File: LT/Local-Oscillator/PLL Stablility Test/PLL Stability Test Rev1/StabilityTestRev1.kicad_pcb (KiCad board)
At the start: 2 copper layers, 12 parts, among them J1 Conn_Coaxial, J11 Conn_Coaxial, J2 Conn_Coaxial, J6 Conn_01x02_Male, J9 Conn_01x03_Male, U3 LMH6611, U4 LMH6611

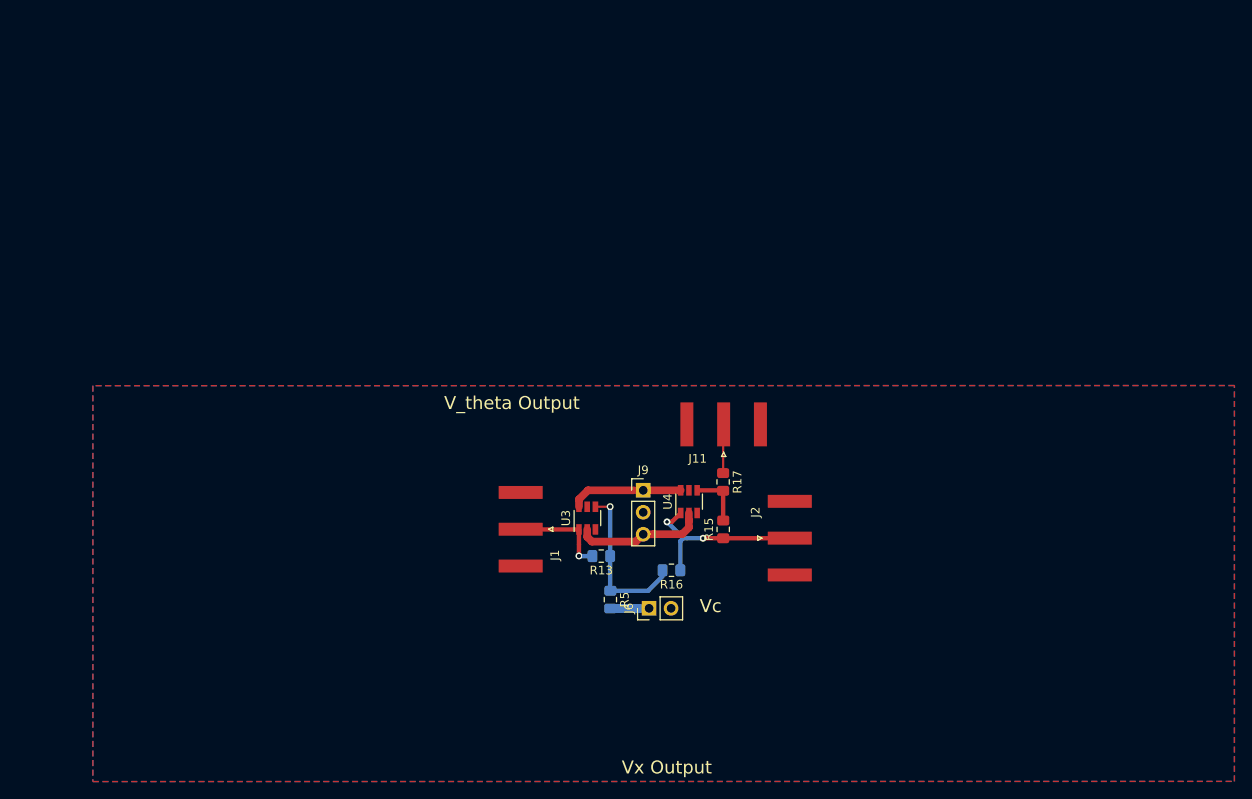
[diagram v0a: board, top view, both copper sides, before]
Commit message: Added Capacitors to the Op-Amp board
I added some capacitors to the Op-Amp test board
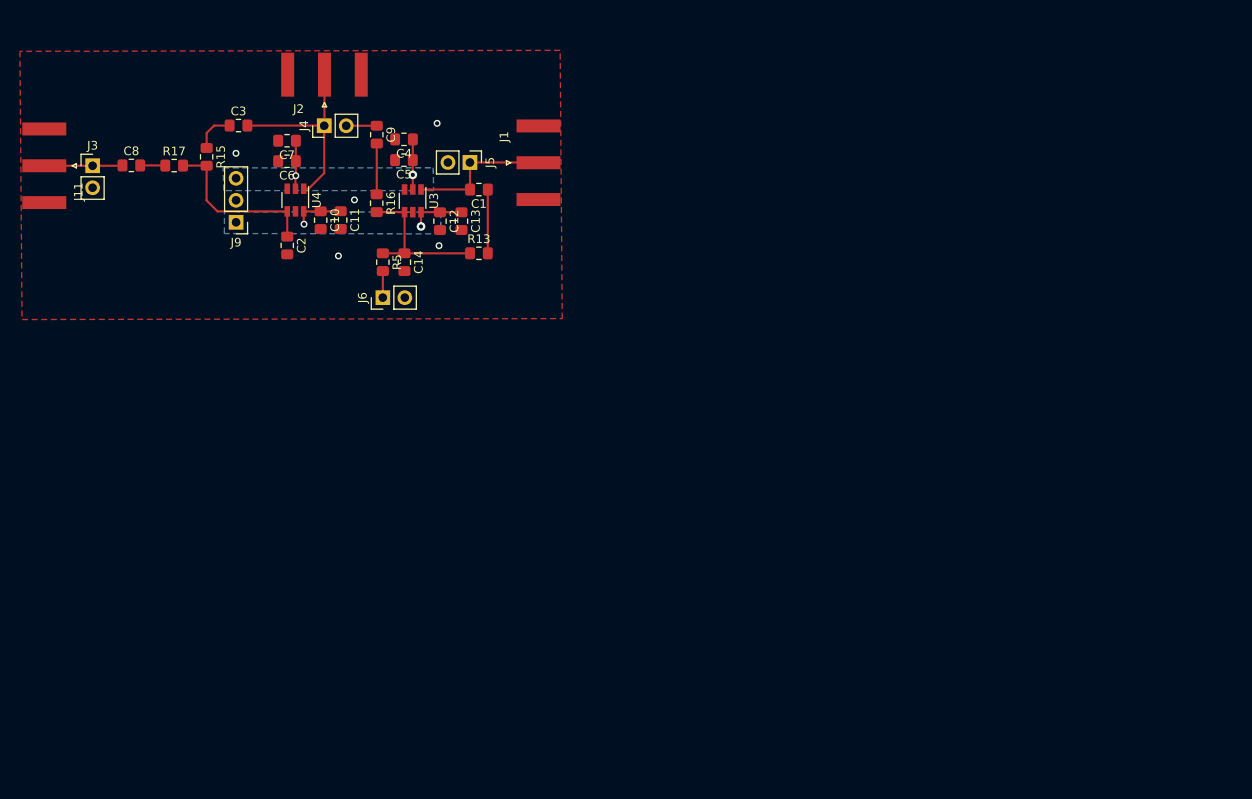
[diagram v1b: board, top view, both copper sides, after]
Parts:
- added C1: 150pF, Capacitor_SMD:C_0805_2012Metric_Pad1.15x1.40mm_HandSolder, F.Cu at (100.7, 53.6)
- added C10: 0.1uF, Capacitor_SMD:C_0805_2012Metric_Pad1.15x1.40mm_HandSolder, F.Cu at (82.4, 57.1)
- added C11: 10uF, Capacitor_SMD:C_0805_2012Metric_Pad1.15x1.40mm_HandSolder, F.Cu at (84.7, 57.1)
- added C12: 0.1uF, Capacitor_SMD:C_0805_2012Metric_Pad1.15x1.40mm_HandSolder, F.Cu at (96.2, 57.2)
- added C13: 10uF, Capacitor_SMD:C_0805_2012Metric_Pad1.15x1.40mm_HandSolder, F.Cu at (98.7, 57.2)
- added C14: 1nF, Capacitor_SMD:C_0805_2012Metric_Pad1.15x1.40mm_HandSolder, F.Cu at (92.1, 62.0)
- added C2: 1nF, Capacitor_SMD:C_0805_2012Metric_Pad1.15x1.40mm_HandSolder, F.Cu at (78.6, 60.0)
- added C3: 150pF, Capacitor_SMD:C_0805_2012Metric_Pad1.15x1.40mm_HandSolder, F.Cu at (72.9, 46.2)
- added C4: 0.1uF, Capacitor_SMD:C_0805_2012Metric_Pad1.15x1.40mm_HandSolder, F.Cu at (92.1, 47.8)
- added C5: 0.1uF, Capacitor_SMD:C_0805_2012Metric_Pad1.15x1.40mm_HandSolder, F.Cu at (92.0, 50.2)
- added C6: 10uF, Capacitor_SMD:C_0805_2012Metric_Pad1.15x1.40mm_HandSolder, F.Cu at (78.5, 50.3)
- added C7: 10uF, Capacitor_SMD:C_0805_2012Metric_Pad1.15x1.40mm_HandSolder, F.Cu at (78.5, 47.9)
- added C8: 1uF, Capacitor_SMD:C_0805_2012Metric_Pad1.15x1.40mm_HandSolder, F.Cu at (60.6, 50.8)
- added C9: 1uF, Capacitor_SMD:C_0805_2012Metric_Pad1.15x1.40mm_HandSolder, F.Cu at (88.9, 47.2)
- added J3: Conn_01x02_Male, Connector_PinHeader_2.54mm:PinHeader_1x02_P2.54mm_Vertical, F.Cu at (56.1, 50.8)
- added J4: Conn_01x02_Male, Connector_PinHeader_2.54mm:PinHeader_1x02_P2.54mm_Vertical, F.Cu at (82.8, 46.2)
- added J5: Conn_01x02_Male, Connector_PinHeader_2.54mm:PinHeader_1x02_P2.54mm_Vertical, F.Cu at (99.7, 50.4)
- moved J11 84.0 mm to (50.5, 50.8), turned to 180 degrees
- moved J2 75.9 mm to (82.9, 40.3), turned to 90 degrees
- moved R15 73.6 mm to (69.3, 49.8), turned to 270 degrees
- moved R17 73.2 mm to (65.5, 50.8), turned to 0 degrees
- moved U4 57.3 mm to (79.5, 54.8), turned to 270 degrees
- moved J9 56.3 mm to (72.7, 57.4), turned to 180 degrees
- moved R16 54.4 mm to (88.9, 55.1), turned to 270 degrees
- moved J6 47.3 mm to (89.6, 66.0)
- moved R5 47.0 mm to (89.6, 62.0)
- moved J1 42.4 mm to (107.6, 50.5), turned to 0 degrees
- moved U3 41.8 mm to (93.1, 54.9), turned to 270 degrees
- moved R13 37.7 mm to (100.7, 60.9), turned to 0 degrees
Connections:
- J1 pad 1: Net-(J1-Pad1) -> Net-(C1-Pad2)
- J11 pad 1: Net-(J11-Pad1) -> Net-(C8-Pad1)
- J2 pad 1: Net-(J2-Pad1) -> Net-(C3-Pad2)
- R13 pad 2: Net-(J1-Pad1) -> Net-(C1-Pad1)
- R15 pad 1: Net-(J2-Pad1) -> Net-(C3-Pad1)
- R16 pad 1: Net-(J2-Pad1) -> Net-(C9-Pad2)
- R17 pad 1: Net-(J11-Pad1) -> Net-(C8-Pad2)
- U3 pad 1: Net-(J1-Pad1) -> Net-(C1-Pad2)
- U4 pad 1: Net-(J2-Pad1) -> Net-(C3-Pad2)
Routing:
- net Net-(C3-Pad2): track 0.00 -> 23.4 mm
- net Net-(J2-Pad1): track 20.8 -> 0.00 mm, vias 2 -> 0
- net Net-(C1-Pad2): track 0.00 -> 16.6 mm
- net Net-(C2-Pad1): track 6.39 -> 19.5 mm
- net Net-(J1-Pad1): track 11.4 -> 0.00 mm, vias 1 -> 0
- net Net-(C8-Pad1): track 0.00 -> 9.05 mm
- net Net-(C1-Pad1): track 0.00 -> 7.36 mm
- net Net-(J11-Pad1): track 6.90 -> 0.00 mm
- net Net-(C9-Pad2): track 0.00 -> 5.87 mm
- net Net-(C3-Pad1): track 0.00 -> 4.74 mm
- net -5V: track 15.2 -> 11.4 mm, vias 0 -> 2
- net Net-(C9-Pad1): track 0.00 -> 3.54 mm
- net Net-(C8-Pad2): track 0.00 -> 2.90 mm
- net Net-(J6-Pad1): track 4.51 -> 3.07 mm
- net +5V: track 13.0 -> 12.1 mm, vias 0 -> 2
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- added copper zone on B.Cu, net +5V
- added copper zone on B.Cu, net -5V
- removed copper zone on B.Cu, net GND
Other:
- board text removed: "V_theta Output"
- board text removed: "Vc"
- board text removed: "Vx Output"

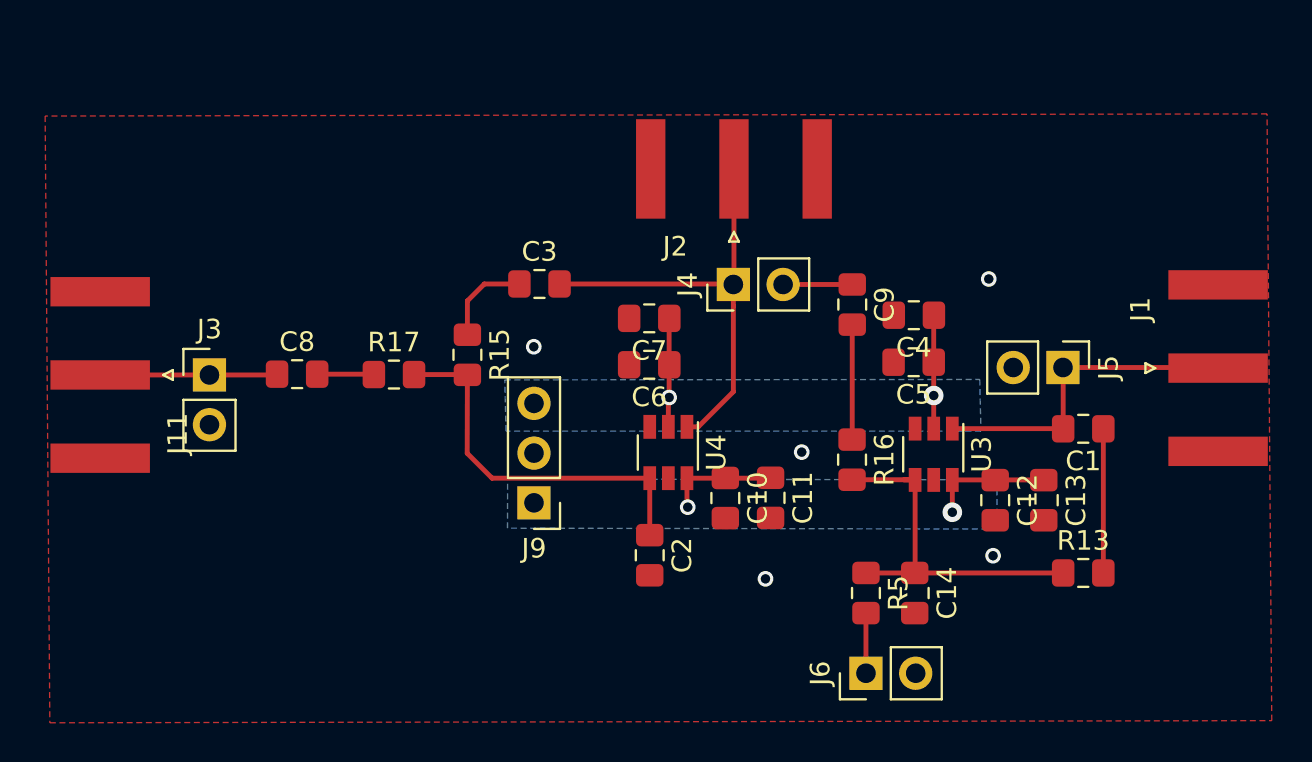
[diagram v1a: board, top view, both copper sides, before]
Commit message: Finished the layout for the Op-Amp Test Board with Capacitors
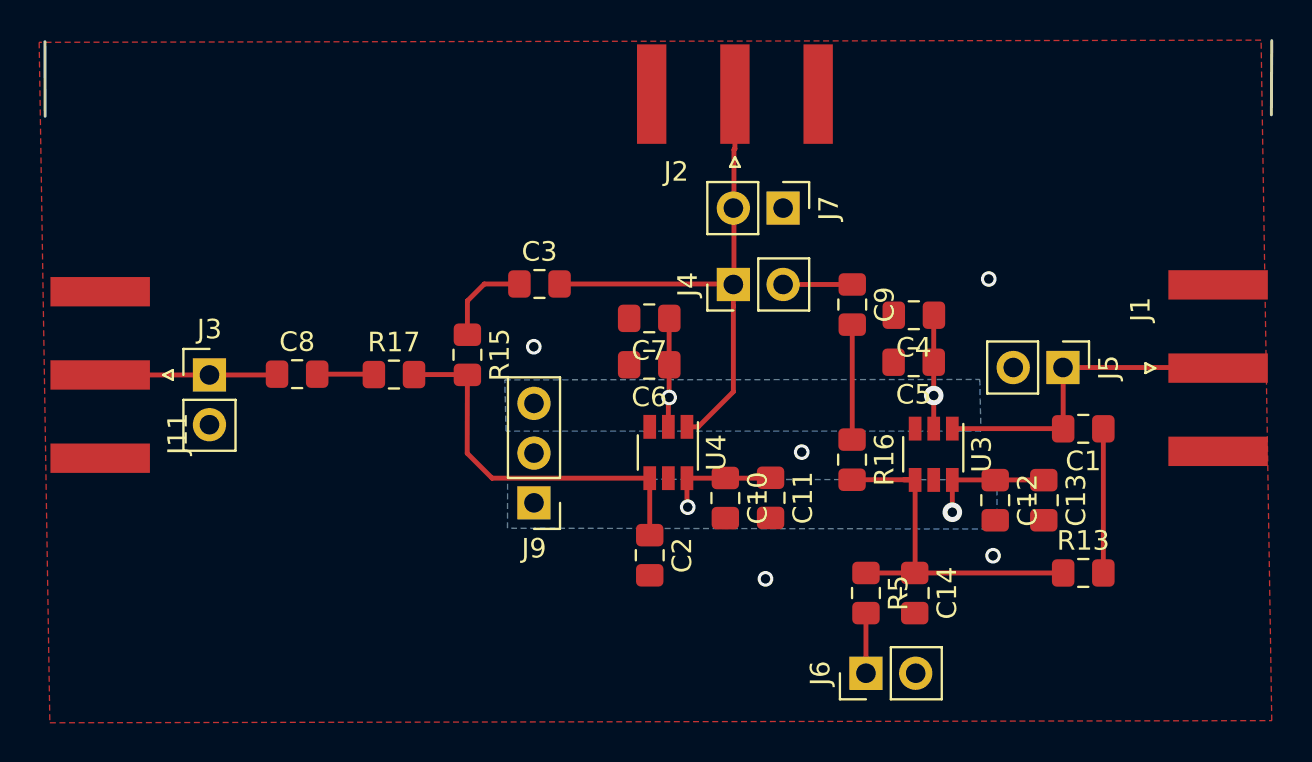
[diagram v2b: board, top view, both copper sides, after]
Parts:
- added J7: Conn_01x02_Male, Connector_PinHeader_2.54mm:PinHeader_1x02_P2.54mm_Vertical, F.Cu at (85.4, 42.3)
- moved J2 3.82 mm to (82.9, 36.5)
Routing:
- net Net-(C3-Pad2): track 23.4 -> 27.2 mm
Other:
- board outline added: 62.6 x 3.9 mm
